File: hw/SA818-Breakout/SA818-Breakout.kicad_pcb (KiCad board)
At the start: 2 copper layers, 56 x 49 mm, 21 parts, among them J1 Conn_Coaxial, J2 Conn_01x02, J3 Conn_01x10, U10 NCP1117-5.0_SOT223

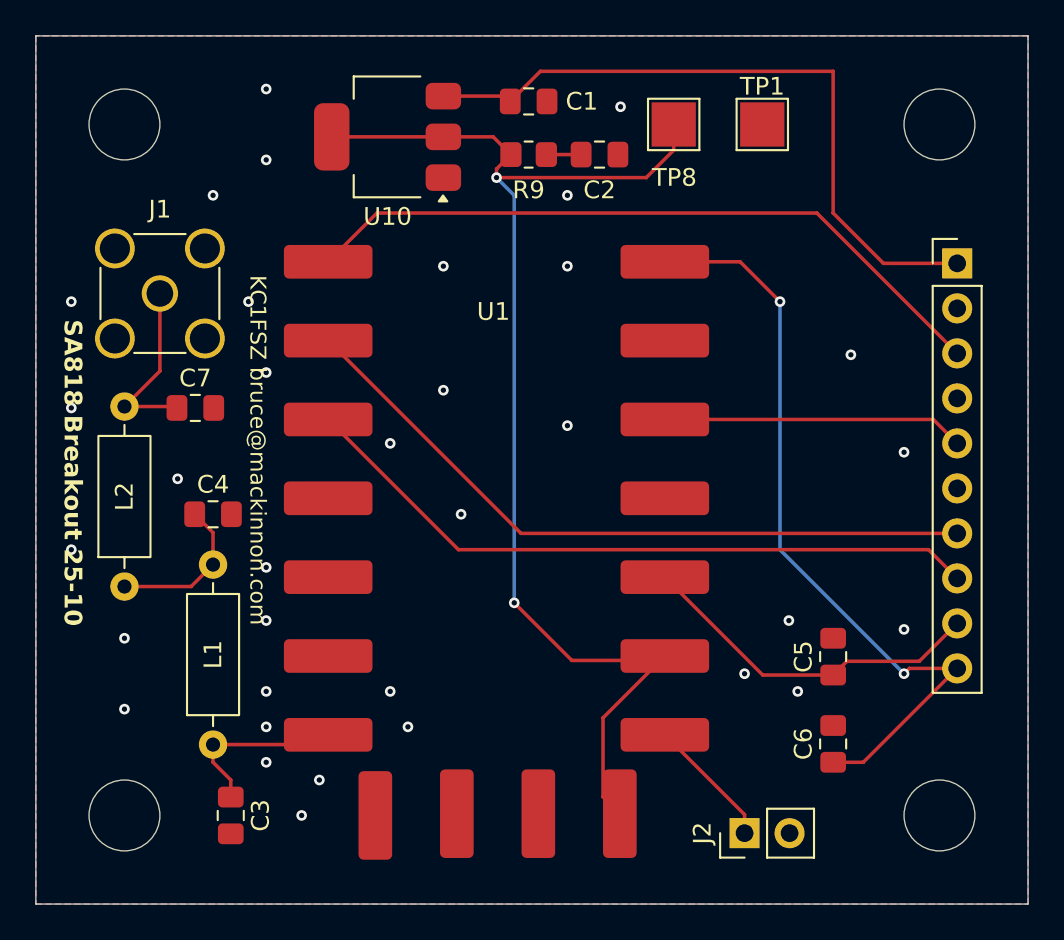
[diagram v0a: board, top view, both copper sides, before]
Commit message: Updated 50ohm traces
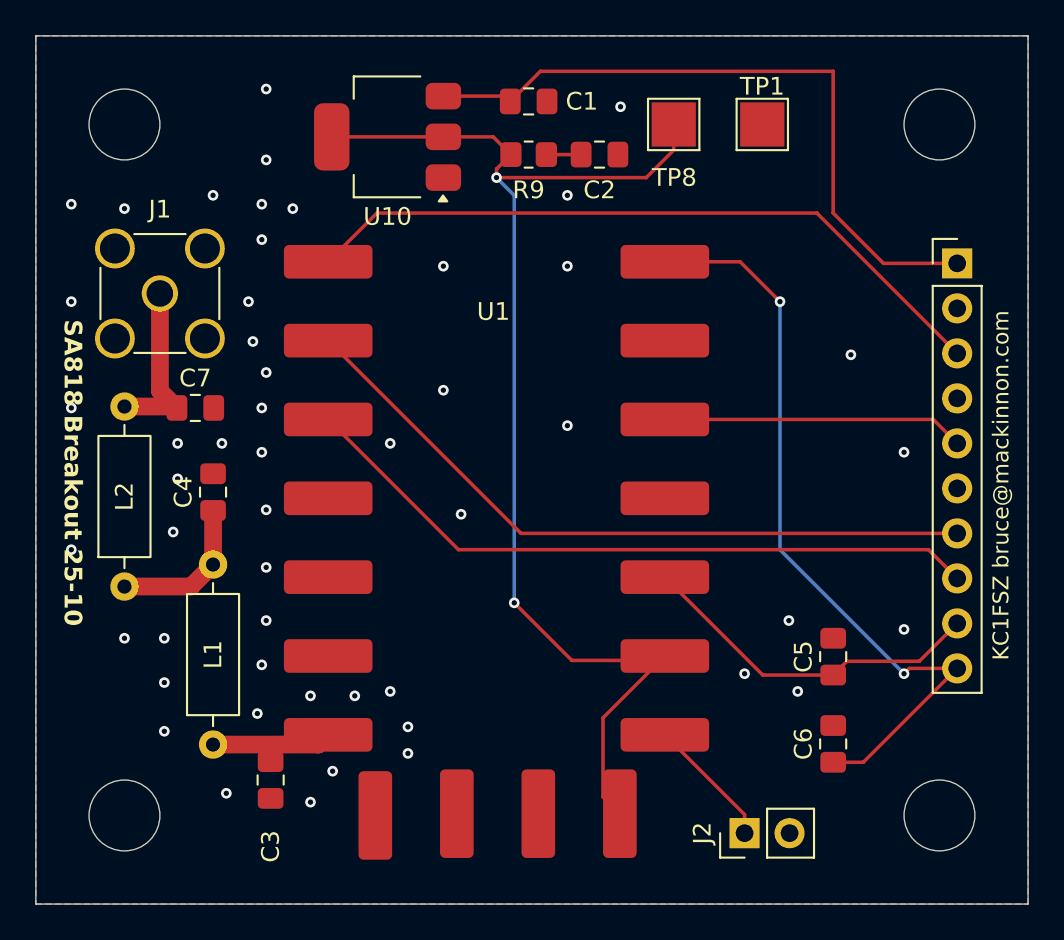
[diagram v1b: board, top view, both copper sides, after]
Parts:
- moved C3 3.01 mm to (116.2, 128.0)
- moved C4 1.25 mm to (113.0, 111.8), turned to 90 degrees
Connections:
- net Net-(C4-Pad1) renamed /LPF1
- net Net-(J1-In) renamed /ANT_OUT
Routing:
- net ANT: track 10.1 -> 6.73 mm
- net GND: vias 34 -> 51
